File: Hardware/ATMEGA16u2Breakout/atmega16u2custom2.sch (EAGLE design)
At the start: 59 parts, among them IC10 74LVC1G125DBV, J3 USB-MICRO B, U1 ATMEGA8U2AU

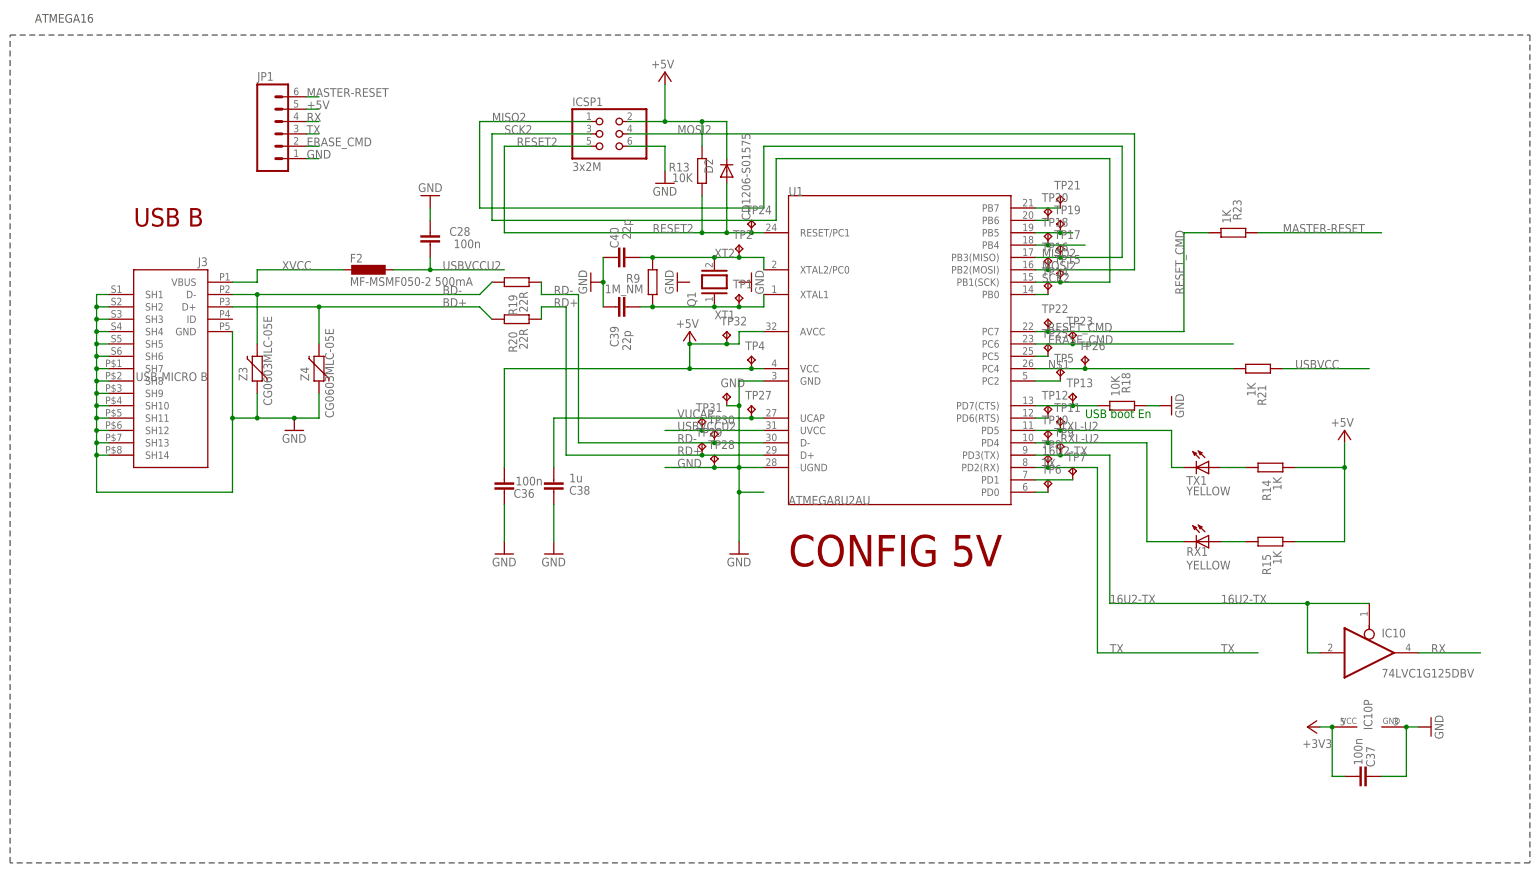
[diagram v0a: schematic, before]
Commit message: ATMEGA16u2 Board Update
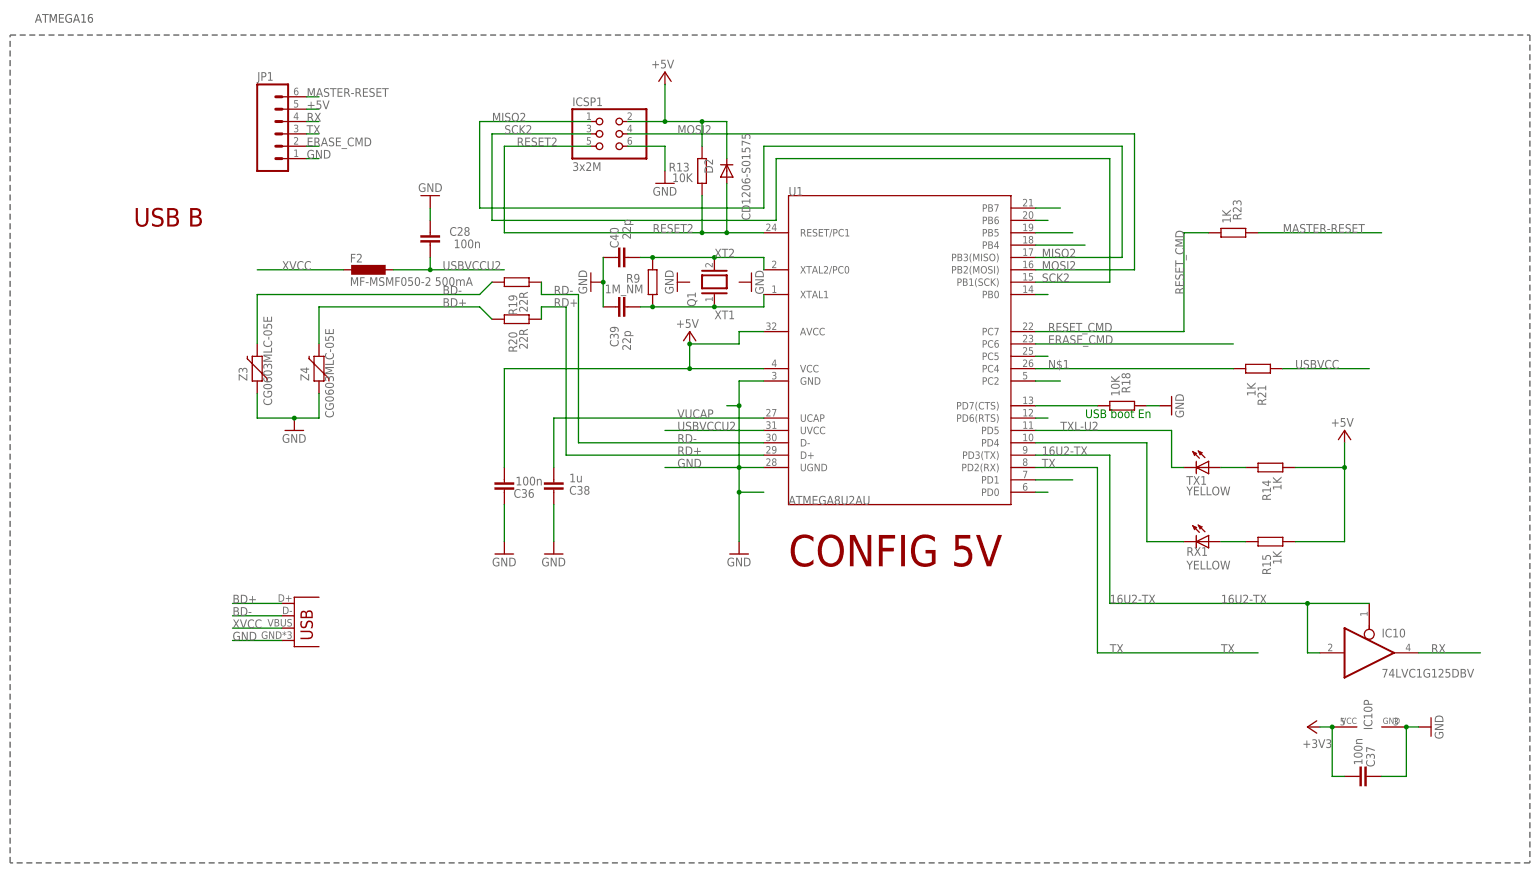
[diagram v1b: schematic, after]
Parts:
- removed GND, TP1, TP10, TP11, TP12, TP13, TP14, TP15, TP16, TP17, TP18, TP19, TP2, TP20, TP21, TP22, TP23, TP24, TP25, TP26, TP27, TP28, TP29, TP30, TP31, TP32, TP4, TP5, TP6, TP7, TP8, TP9: TPB1,27, testpad:TPB1,27
- removed J3: USB-MICRO B, SmartPrj:MYCON2_USB-MINI-B
- added JP2: USB-MICROB, SparkFun-Connectors:USB-MICROB
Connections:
- net +5V: no longer TP32.TP, TP4.TP
- net 16U2-TX: no longer TP9.TP
- net 8PB4: no longer TP18.TP
- net 8PB5: no longer TP19.TP
- net 8PB6: no longer TP20.TP
- net BD+: now also JP2.D+; no longer J3.D+
- net BD-: now also JP2.D-; no longer J3.D-
- net DTR: no longer TP13.TP
- net ERASE_CMD: no longer TP23.TP
- net GND: now also JP2.GND; no longer GND.TP, J3.GND, J3.SH1, J3.SH10, J3.SH11, J3.SH12, J3.SH13, J3.SH14, J3.SH2, J3.SH3, J3.SH4, J3.SH5, J3.SH6, J3.SH7, J3.SH8, J3.SH9, TP28.TP
- net MISO2: no longer TP17.TP
- net MOSI2: no longer TP16.TP
- net N$1: no longer TP26.TP
- net N$2: no longer TP5.TP
- net N$3: no longer TP6.TP
- net N$5: no longer TP7.TP
- net N$6: no longer TP12.TP
- net N$7: no longer TP25.TP
- net N$8: no longer TP14.TP
- net N$9: no longer TP21.TP
- net RD+: no longer TP29.TP
- net RD-: no longer TP30.TP
- net RESET2: no longer TP24.TP
- net RESET_CMD: no longer TP22.TP
- net RXL-U2: no longer TP10.TP
- net SCK2: no longer TP15.TP
- net TX: no longer TP8.TP
- net TXL-U2: no longer TP11.TP
- net USBVCCU2: no longer TP31.TP
- net VUCAP: no longer TP27.TP
- net XT1: no longer TP1.TP
- net XT2: no longer TP2.TP
- net XVCC: now also JP2.VBUS; no longer J3.VBUS

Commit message: Updated atmega16 breakout board, and gerbers
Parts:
- removed R21, R23: 1K, SmartPrj:R-EU_R0805
- removed R9: 1M_NM, SmartPrj:R-EU_R0805
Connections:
- removed net N$1: R21.1, U1.PC4
- removed net RESET_CMD: R23.1, U1.PC7
- removed net USBVCC: R21.2
- removed net USBVCCU2: C28.1, F2.1, U1.UVCC
- net +5V: now also C28.1, F2.1, JP1.1, U1.UVCC; no longer JP1.5
- net GND: now also JP1.6; no longer JP1.1
- net MASTER-RESET: now also JP1.3, U1.PC7; no longer JP1.6, R23.2
- net RX: now also JP1.5; no longer JP1.4
- net TX: now also JP1.4; no longer JP1.3
- net XT1: no longer R9.1
- net XT2: no longer R9.2
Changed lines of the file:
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@@
 <part name="Z3" library="varistor" deviceset="VARISTOR" device="CN0603" value="CG0603MLC-05E"/>
 <part name="Z4" library="varistor" deviceset="VARISTOR" device="CN0603" value="CG0603MLC-05E"/>
-<part name="R9" library="SmartPrj" deviceset="R-EU_" device="R0805" value="1M_NM"/>
 <part name="C39" library="SmartPrj" deviceset="C-EU" device="C0805" value="22p"/>
 <part name="C40" library="SmartPrj" deviceset="C-EU" device="C0805" value="22p"/>
@@
 <part name="R20" library="SmartPrj" deviceset="R-EU_" device="R0805" value="22R"/>
 <part name="GND11" library="supply1" deviceset="GND" device=""/>
-<part name="R21" library="SmartPrj" deviceset="R-EU_" device="R0805" value="1K"/>
 <part name="P+3" library="supply1" deviceset="+5V" device=""/>
 <part name="P+5" library="supply1" deviceset="+5V" device=""/>
 <part name="IC10" library="74xx-little-us" deviceset="74*1G125" device="DBV" technology="LVC" value="74LVC1G125DBV"/>
-<part name="R23" library="SmartPrj" deviceset="R-EU_" device="R0805" value="1K"/>
 <part name="GND30" library="supply1" deviceset="GND" device=""/>
 <part name="GND38" library="supply1" deviceset="GND" device=""/>
@@
 <attribute name="VALUE" x="-21.59" y="20.32" size="1.778" layer="96" rot="MR90"/>
 </instance>
-<instance part="R9" gate="G$1" x="45.72" y="48.26" smashed="yes" rot="R90">
-<attribute name="NAME" x="43.18" y="49.9364" size="1.778" layer="95" rot="R180"/>
-<attribute name="VALUE" x="43.815" y="47.752" size="1.778" layer="96" rot="R180"/>
-</instance>
 <instance part="C39" gate="G$1" x="40.64" y="43.18" smashed="yes" rot="MR90">
 <attribute name="NAME" x="38.735" y="39.243" size="1.778" layer="95" rot="MR270"/>
@@
 </instance>
 <instance part="GND11" gate="1" x="152.4" y="22.86" rot="R90"/>
-<instance part="R21" gate="G$1" x="170.18" y="30.48" smashed="yes">
-<attribute name="NAME" x="171.8564" y="22.86" size="1.778" layer="95" rot="R90"/>
-<attribute name="VALUE" x="169.672" y="24.765" size="1.778" layer="96" rot="R90"/>
-</instance>
 <instance part="P+3" gate="1" x="53.34" y="38.1" smashed="yes">
 <attribute name="VALUE" x="55.245" y="40.64" size="1.778" layer="96" rot="R180"/>
@@
 </instance>
 <instance part="IC10" gate="A" x="193.04" y="-27.94"/>
-<instance part="R23" gate="G$1" x="165.1" y="58.42" smashed="yes">
-<attribute name="NAME" x="166.7764" y="60.96" size="1.778" layer="95" rot="R90"/>
-<attribute name="VALUE" x="164.592" y="60.325" size="1.778" layer="96" rot="R90"/>
-</instance>
 <instance part="GND30" gate="1" x="50.8" y="48.26" rot="R270"/>
 <instance part="GND38" gate="1" x="66.04" y="48.26" rot="R90"/>
@@
 </segment>
 <segment>
-<pinref part="JP1" gate="G$1" pin="5"/>
-<wire x1="-25.4" y1="83.82" x2="-22.86" y2="83.82" width="0.1524" layer="91"/>
-<label x="-25.4" y="83.82" size="1.778" layer="95"/>
+<wire x1="15.24" y1="50.8" x2="0" y2="50.8" width="0.1524" layer="91"/>
+<wire x1="0" y1="53.34" x2="0" y2="50.8" width="0.1524" layer="91"/>
+<wire x1="0" y1="50.8" x2="-7.62" y2="50.8" width="0.1524" layer="91"/>
+<junction x="0" y="50.8"/>
+<label x="2.54" y="50.8" size="1.778" layer="95"/>
+<pinref part="C28" gate="G$1" pin="1"/>
+<pinref part="F2" gate="G$1" pin="1"/>
+</segment>
+<segment>
+<wire x1="68.58" y1="17.78" x2="48.26" y2="17.78" width="0.1524" layer="91"/>
+<label x="50.8" y="17.78" size="1.778" layer="95"/>
+<pinref part="U1" gate="G$1" pin="UVCC"/>
+</segment>
+<segment>
+<pinref part="JP1" gate="G$1" pin="1"/>
+<wire x1="-25.4" y1="73.66" x2="-22.86" y2="73.66" width="0.1524" layer="91"/>
+<label x="-25.4" y="73.66" size="1.778" layer="95"/>
 </segment>
 </net>
@@
 </segment>
 <segment>
-<pinref part="JP1" gate="G$1" pin="1"/>
-<wire x1="-25.4" y1="73.66" x2="-22.86" y2="73.66" width="0.1524" layer="91"/>
-<label x="-25.4" y="73.66" size="1.778" layer="95"/>
-</segment>
-<segment>
 <wire x1="-30.48" y1="-25.4" x2="-40.64" y2="-25.4" width="0.1524" layer="91"/>
 <pinref part="JP2" gate="G$1" pin="GND"/>
 <label x="-40.64" y="-25.4" size="1.778" layer="95"/>
+</segment>
+<segment>
+<pinref part="JP1" gate="G$1" pin="6"/>
+<wire x1="-25.4" y1="86.36" x2="-22.86" y2="86.36" width="0.1524" layer="91"/>
+<label x="-25.4" y="86.36" size="1.778" layer="95"/>
 </segment>
 </net>
@@
 </segment>
 </net>
-<net name="USBVCC" class="0">
-<segment>
-<pinref part="R21" gate="G$1" pin="2"/>
-<wire x1="175.26" y1="30.48" x2="193.04" y2="30.48" width="0.1524" layer="91"/>
-<label x="177.8" y="30.48" size="1.778" layer="95"/>
-</segment>
-</net>
 <net name="RX" class="0">
 <segment>
@@
 </segment>
 <segment>
-<pinref part="JP1" gate="G$1" pin="4"/>
-<wire x1="-25.4" y1="81.28" x2="-22.86" y2="81.28" width="0.1524" layer="91"/>
-<label x="-25.4" y="81.28" size="1.778" layer="95"/>
+<pinref part="JP1" gate="G$1" pin="5"/>
+<wire x1="-25.4" y1="83.82" x2="-22.86" y2="83.82" width="0.1524" layer="91"/>
+<label x="-25.4" y="83.82" size="1.778" layer="95"/>
 </segment>
 </net>
@@
 </segment>
 <segment>
+<pinref part="JP1" gate="G$1" pin="4"/>
+<wire x1="-25.4" y1="81.28" x2="-22.86" y2="81.28" width="0.1524" layer="91"/>
+<label x="-25.4" y="81.28" size="1.778" layer="95"/>
+</segment>
+</net>
+<net name="MASTER-RESET" class="0">
+<segment>
+<label x="154.94" y="45.72" size="1.778" layer="95" rot="R90"/>
+<wire x1="124.46" y1="38.1" x2="154.94" y2="38.1" width="0.1524" layer="91"/>
+<wire x1="154.94" y1="38.1" x2="154.94" y2="58.42" width="0.1524" layer="91"/>
+<label x="127" y="38.1" size="1.778" layer="95"/>
+<pinref part="U1" gate="G$1" pin="PC7"/>
+<label x="175.26" y="58.42" size="1.778" layer="95"/>
+<wire x1="154.94" y1="58.42" x2="195.58" y2="58.42" width="0.1524" layer="91"/>
+</segment>
+<segment>
 <pinref part="JP1" gate="G$1" pin="3"/>
 <wire x1="-25.4" y1="78.74" x2="-22.86" y2="78.74" width="0.1524" layer="91"/>
 <label x="-25.4" y="78.74" size="1.778" layer="95"/>
-</segment>
-</net>
-<net name="MASTER-RESET" class="0">
-<segment>
-<label x="175.26" y="58.42" size="1.778" layer="95"/>
-<pinref part="R23" gate="G$1" pin="2"/>
-<wire x1="170.18" y1="58.42" x2="195.58" y2="58.42" width="0.1524" layer="91"/>
-</segment>
-<segment>
-<pinref part="JP1" gate="G$1" pin="6"/>
-<wire x1="-25.4" y1="86.36" x2="-22.86" y2="86.36" width="0.1524" layer="91"/>
-<label x="-25.4" y="86.36" size="1.778" layer="95"/>
 </segment>
 </net>
@@
 <segment>
 <wire x1="68.58" y1="53.34" x2="58.42" y2="53.34" width="0.1524" layer="91"/>
-<wire x1="58.42" y1="53.34" x2="45.72" y2="53.34" width="0.1524" layer="91"/>
-<wire x1="45.72" y1="53.34" x2="43.18" y2="53.34" width="0.1524" layer="91"/>
+<wire x1="58.42" y1="53.34" x2="43.18" y2="53.34" width="0.1524" layer="91"/>
 <wire x1="68.58" y1="53.34" x2="68.58" y2="50.8" width="0.1524" layer="91"/>
-<junction x="45.72" y="53.34"/>
 <label x="58.42" y="53.34" size="1.778" layer="95"/>
 <pinref part="C40" gate="G$1" pin="1"/>
-<pinref part="R9" gate="G$1" pin="2"/>
 <pinref part="U1" gate="G$1" pin="XTAL2/PC0"/>
 <pinref part="Q1" gate="G$1" pin="2"/>
@@
 <net name="XT1" class="0">
 <segment>
-<wire x1="45.72" y1="43.18" x2="43.18" y2="43.18" width="0.1524" layer="91"/>
 <wire x1="68.58" y1="43.18" x2="58.42" y2="43.18" width="0.1524" layer="91"/>
-<wire x1="58.42" y1="43.18" x2="45.72" y2="43.18" width="0.1524" layer="91"/>
+<wire x1="58.42" y1="43.18" x2="43.18" y2="43.18" width="0.1524" layer="91"/>
 <wire x1="68.58" y1="43.18" x2="68.58" y2="45.72" width="0.1524" layer="91"/>
-<junction x="45.72" y="43.18"/>
 <label x="58.42" y="40.64" size="1.778" layer="95"/>
 <pinref part="C39" gate="G$1" pin="1"/>
-<pinref part="R9" gate="G$1" pin="1"/>
 <pinref part="U1" gate="G$1" pin="XTAL1"/>
 <pinref part="Q1" gate="G$1" pin="1"/>
@@
 <pinref part="U1" gate="G$1" pin="PB4"/>
 <wire x1="124.46" y1="55.88" x2="134.62" y2="55.88" width="0.1524" layer="91"/>
-</segment>
-</net>
-<net name="RESET_CMD" class="0">
-<segment>
-<label x="154.94" y="45.72" size="1.778" layer="95" rot="R90"/>
-<wire x1="124.46" y1="38.1" x2="154.94" y2="38.1" width="0.1524" layer="91"/>
-<wire x1="154.94" y1="38.1" x2="154.94" y2="58.42" width="0.1524" layer="91"/>
-<label x="127" y="38.1" size="1.778" layer="95"/>
-<pinref part="R23" gate="G$1" pin="1"/>
-<wire x1="160.02" y1="58.42" x2="154.94" y2="58.42" width="0.1524" layer="91"/>
-<pinref part="U1" gate="G$1" pin="PC7"/>
 </segment>
 </net>
@@
 </segment>
 </net>
-<net name="N$1" class="0">
-<segment>
-<pinref part="R21" gate="G$1" pin="1"/>
-<wire x1="165.1" y1="30.48" x2="124.46" y2="30.48" width="0.1524" layer="91"/>
-<label x="127" y="30.48" size="1.778" layer="95"/>
-<pinref part="U1" gate="G$1" pin="PC4"/>
-</segment>
-</net>
 <net name="VUCAP" class="0">
 <segment>
@@
 </segment>
 </net>
-<net name="USBVCCU2" class="0">
-<segment>
-<wire x1="15.24" y1="50.8" x2="0" y2="50.8" width="0.1524" layer="91"/>
-<wire x1="0" y1="53.34" x2="0" y2="50.8" width="0.1524" layer="91"/>
-<wire x1="0" y1="50.8" x2="-7.62" y2="50.8" width="0.1524" layer="91"/>
-<junction x="0" y="50.8"/>
-<label x="2.54" y="50.8" size="1.778" layer="95"/>
-<pinref part="C28" gate="G$1" pin="1"/>
-<pinref part="F2" gate="G$1" pin="1"/>
-</segment>
-<segment>
-<wire x1="68.58" y1="17.78" x2="48.26" y2="17.78" width="0.1524" layer="91"/>
-<label x="50.8" y="17.78" size="1.778" layer="95"/>
-<pinref part="U1" gate="G$1" pin="UVCC"/>
-</segment>
-</net>
